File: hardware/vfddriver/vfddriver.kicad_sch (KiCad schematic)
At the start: 20 parts, among them J1 Connection Header, J2 HV EN, U1 IVL2-5_7, U2 LM2733YMF, U4 HV5812WG, U5 ATtiny412-SS

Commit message: hw: [WIP] begin rework vfddriver with hbridge filament
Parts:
- removed J2: HV EN, Connector_PinHeader_2.54mm:PinHeader_2x01_P2.54mm_Vertical, symbol Connector_Generic:Conn_02x01
- removed RV1: 10kΩ, Potentiometer_THT:Potentiometer_Bourns_3266W_Vertical, symbol Device:RTRIM
- removed U2: LM2733YMF, Package_TO_SOT_SMD:SOT-23-5, symbol Regulator_Switching:LM2733YMF
- removed U5: ATtiny412-SS, Package_SO:SOIC-8_3.9x4.9mm_P1.27mm, symbol MCU_Microchip_ATtiny:ATtiny412-SS
- added C4: 10µF, Capacitor_SMD:C_0805_2012Metric_Pad1.18x1.45mm_HandSolder, symbol Device:C_Small
- added L2: 10µH, Inductor_SMD:L_1210_3225Metric_Pad1.42x2.65mm_HandSolder, symbol Device:L_Small
- added R4: 10kΩ, Resistor_SMD:R_0805_2012Metric_Pad1.20x1.40mm_HandSolder, symbol Device:R_Small
- added R5, R6: 0Ω, Resistor_SMD:R_1206_3216Metric_Pad1.30x1.75mm_HandSolder, symbol Device:R_Small
- added RV1: Trimmer, Potentiometer_THT:Potentiometer_Bourns_3266W_Vertical, symbol Device:R_POT_Small
- added U2: ATtiny414-SS, Package_SO:SOIC-14_3.9x8.7mm_P1.27mm, symbol MCU_Microchip_ATtiny:ATtiny414-SS
- added U3: LM2733YMF, Package_TO_SOT_SMD:SOT-23-5, symbol Regulator_Switching:LM2733YMF
- added U5: ZXBM5210-S, Package_SO:SOIC-8_3.9x4.9mm_P1.27mm, symbol Driver_Motor:ZXBM5210-S
- H1, H2, H3, H4: value MountingHole_Pad -> Mount
- J1: value Connection Header -> Header
- R1: value 47kΩ -> 10kΩ
- R14: value 47kΩ -> 10kΩ; footprint Resistor_SMD:R_0805_2012Metric_Pad1.15x1.40mm_HandSolder -> Resistor_SMD:R_0805_2012Metric_Pad1.20x1.40mm_HandSolder
- U4: symbol HV5812:HV5812WG -> chronovfd:HV5812WG
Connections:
- net 5V is gone; now on net +5V: C1.1, L1.1
- net +5V: now also R1.1, U4.28 (VDD), U2.1 (VCC), U3.5 (VIN)
- net FILAMENT+: now also R6.1
- net FILAMENT-: now also R5.1
- net G1: now also U4.9 (HVOUT14)
- net G2: now also U4.26 (HVOUT1)
- net G3: now also U4.24 (HVOUT3)
- net G4: now also U4.21 (HVOUT6)
- net G5: now also U4.17 (HVOUT10)
- net GND: now also U4.14 (GND), C4.2, RV1.3, U2.14 (GND), U3.2 (GND), U5.8 (GND); no longer R1.2
- net HV: now also U4.1 (VPP_HV), R4.1
- net HV_BLANK: now also U4.13 (BLANKING)
- net HV_CLOCK: now also U4.15 (CLOCK)
- net HV_DATA: now also U4.27 (DATA_IN)
- net HV_STROBE: now also U4.16 (STROBE)
- net UPDI: now also U2.10 (~{RESET}/PA0)
- net a: now also U4.18 (HVOUT9)
- net b: now also U4.20 (HVOUT7)
- net c: now also U4.25 (HVOUT2)
- net d: now also U4.22 (HVOUT5)
- net db: now also U4.23 (HVOUT4)
- net dt: now also U4.10 (HVOUT13)
- net e: now also U4.12 (HVOUT11)
- net f: now also U4.19 (HVOUT8)
- net g: now also U4.11 (HVOUT12)
- net ~{HV_SHDN}: now also R1.2, U3.4 (EN)
- net at D1.2 (A), L1.2: now also U3.1 (SW)
- net at R3.1: now also R4.2
- net at C2.1, R2.2, R3.2: now also U3.3 (FB)
- new net: R5.2, U5.1 (OUT1)
- new net: C4.1, L2.2, U5.2 (VM)
- new net: R6.2, U5.7 (OUT2)
- new net: L2.1, RV1.1, U5.3 (VDD)
- new net: RV1.2, U5.6 (VREF)
- new net FIL_FWD: U5.4 (FWD)
- new net FIL_REV: U5.5 (REV)
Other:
- note added: "(alternatives: BD6211F-E2, BA6287F-E2)"
- moved on the sheet: H1, H2, H3, H4, J1, R14, U1

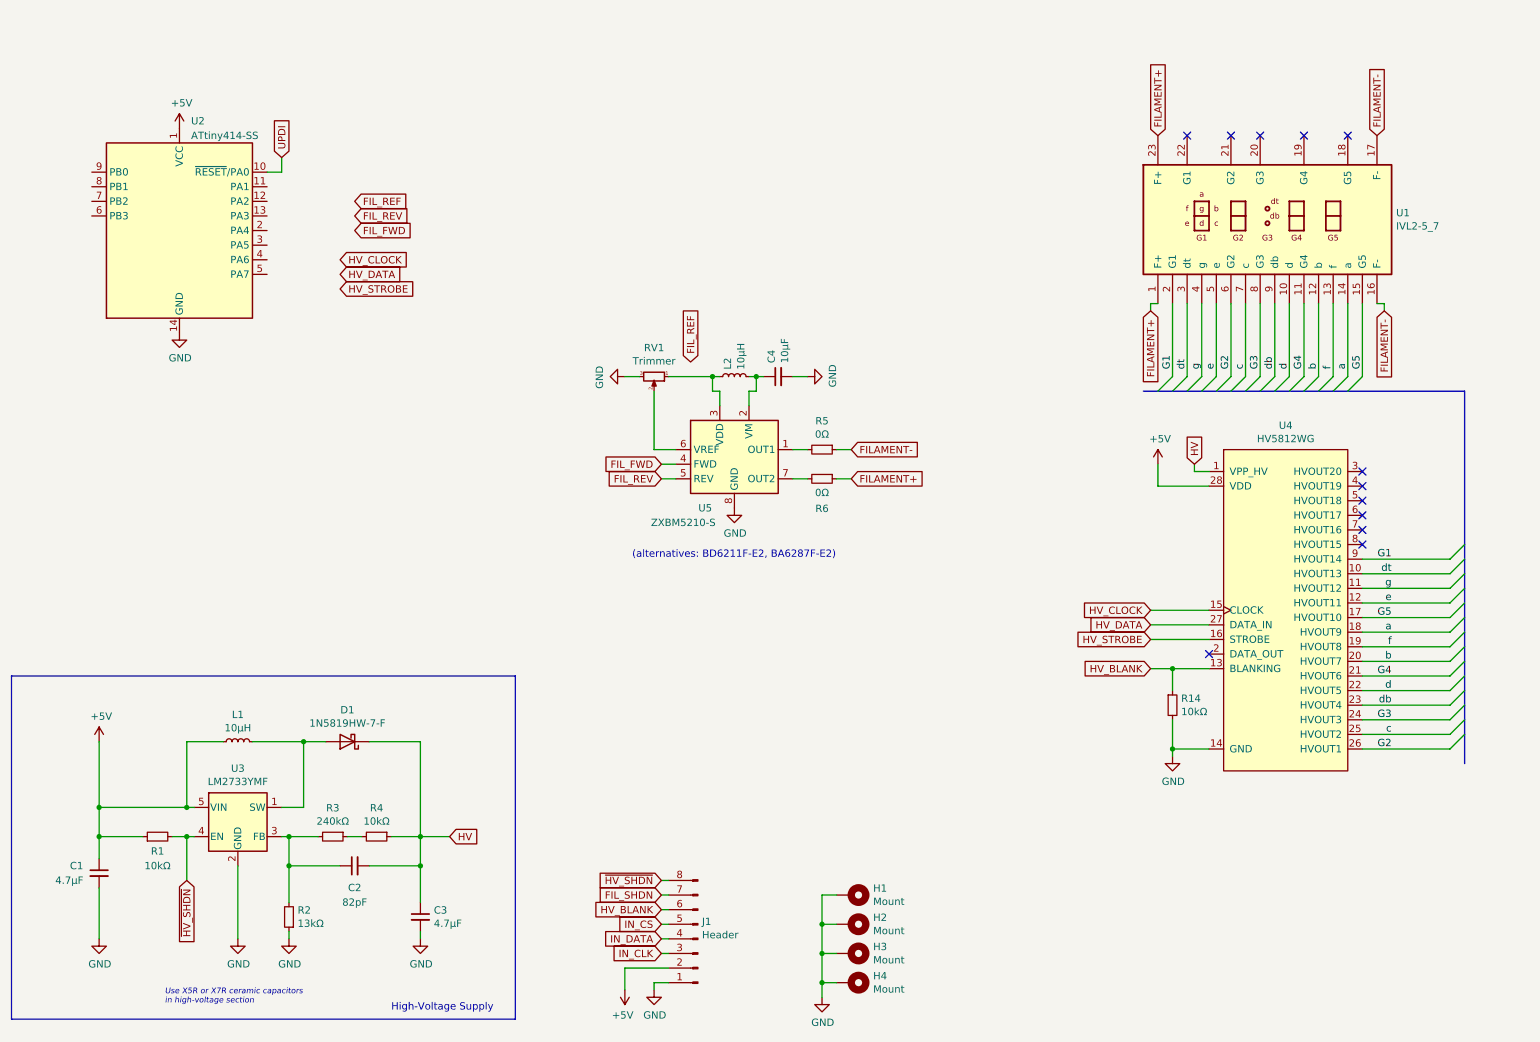
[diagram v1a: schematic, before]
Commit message: hw: finished redesign of vfddriver frontplate
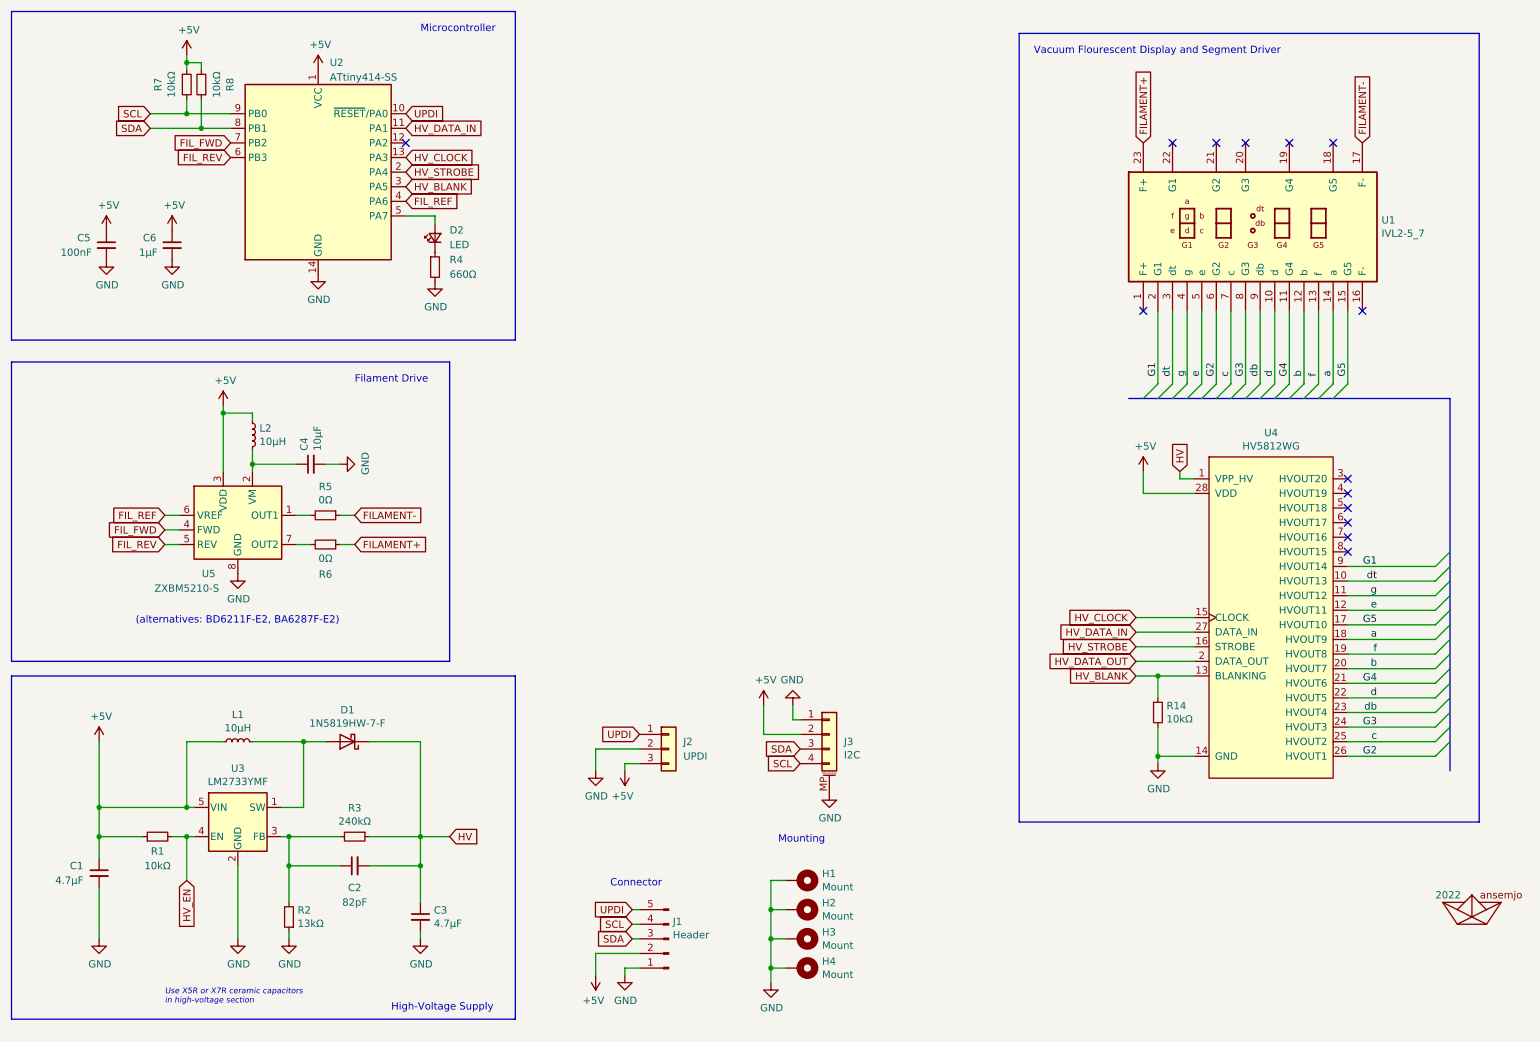
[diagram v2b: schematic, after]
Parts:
- removed RV1: Trimmer, Potentiometer_THT:Potentiometer_Bourns_3266W_Vertical, symbol Device:R_POT_Small
- added A1: 2022, ansemjo:ahoi-mask, symbol ansemjo:ahoi
- added C5: 100nF, Capacitor_SMD:C_0805_2012Metric_Pad1.18x1.45mm_HandSolder, symbol Device:C_Small
- added C6: 1µF, Capacitor_SMD:C_0805_2012Metric_Pad1.18x1.45mm_HandSolder, symbol Device:C_Small
- added D2: LED, LED_SMD:LED_0805_2012Metric_Pad1.15x1.40mm_HandSolder, symbol Device:LED_Small
- added J2: UPDI, ansemjo:UPDI_PogoProg_pinHoles, symbol Connector_Generic:Conn_01x03
- added J3: I2C, Connector_JST:JST_SH_SM04B-SRSS-TB_1x04-1MP_P1.00mm_Horizontal, symbol Connector_Generic_MountingPin:Conn_01x04_MountingPin
- added R7, R8: 10kΩ, Resistor_SMD:R_0805_2012Metric_Pad1.20x1.40mm_HandSolder, symbol Device:R_Small
- J1: footprint Connector_PinHeader_2.54mm:PinHeader_1x08_P2.54mm_Vertical -> Connector_PinHeader_2.54mm:PinHeader_1x05_P2.54mm_Vertical; symbol Connector:Conn_01x08_Male -> Connector:Conn_01x05_Male
- R4: value 10kΩ -> 660Ω; Digi-Key PN 311-10.0KCRCT-ND -> (none); MPN RC0805FR-0710KL -> (none); Mfg Yageo -> (none)
- U3: footprint Package_TO_SOT_SMD:SOT-23-5 -> Package_TO_SOT_SMD:SOT-23-5_HandSoldering
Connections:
- net HV_DATA is gone; now on net HV_DATA_IN: U4.27 (DATA_IN)
- net IN_CLK is gone; now on net SDA: J1.3 (Pin_3)
- net IN_CS is gone; now on net UPDI: J1.5 (Pin_5)
- net IN_DATA is gone; now on net SCL: J1.4 (Pin_4)
- net +5V: now also L2.1, U5.3 (VDD), C5.1, C6.1, J2.3 (Pin_3), J3.2 (Pin_2), R7.1, R8.2
- net FILAMENT+: no longer U1.1 (F+)
- net FILAMENT-: no longer U1.16 (F-)
- net FIL_FWD: now also U2.7 (PB2)
- net FIL_REF: now also U2.4 (PA6), U5.6 (VREF)
- net FIL_REV: now also U2.6 (PB3)
- net GND: now also R4.2, C5.2, C6.2, J2.2 (Pin_2), J3.1 (Pin_1), J3.MP (MountPin)
- net HV: now also R3.1; no longer R4.1
- net HV_BLANK: now also U2.3 (PA5); no longer J1.6 (Pin_6)
- net HV_CLOCK: now also U2.13 (PA3)
- net HV_STROBE: now also U2.2 (PA4)
- net UPDI: now also J2.1 (Pin_1)
- net HV_DATA_OUT: now reaches U4.2 (DATA_OUT)
- net HV_DATA_IN: now reaches U2.11 (PA1)
- net at U2.5 (PA7): now also D2.2 (A)
- net SDA: now reaches U2.8 (PB1)
- net SDA: now also J3.3 (Pin_3), R8.1
- net SCL: now reaches U2.9 (PB0)
- net SCL: now also J3.4 (Pin_4), R7.2
- removed net FIL_SHDN: J1.7 (Pin_7)
- net ~{HV_SHDN} renamed HV_EN
- net HV_EN: no longer J1.8 (Pin_8)
- new net: D2.1 (K), R4.1
- no-connect marks 12 -> 14
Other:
- note added: "Connector"
- note added: "Filament Drive"
- note added: "Microcontroller"
- note added: "Mounting"
- note added: "Vacuum Flourescent Display and Segment Driver"
- moved on the sheet: C4, H1, H2, H3, H4, L2, R14, R3, R5, R6, U1, U2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
